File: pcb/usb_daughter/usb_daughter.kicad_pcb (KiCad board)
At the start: 2 copper layers, 26.2 x 18 mm, 6 parts, among them J1 USB-A1VSB6, J2 USB_B_Micro

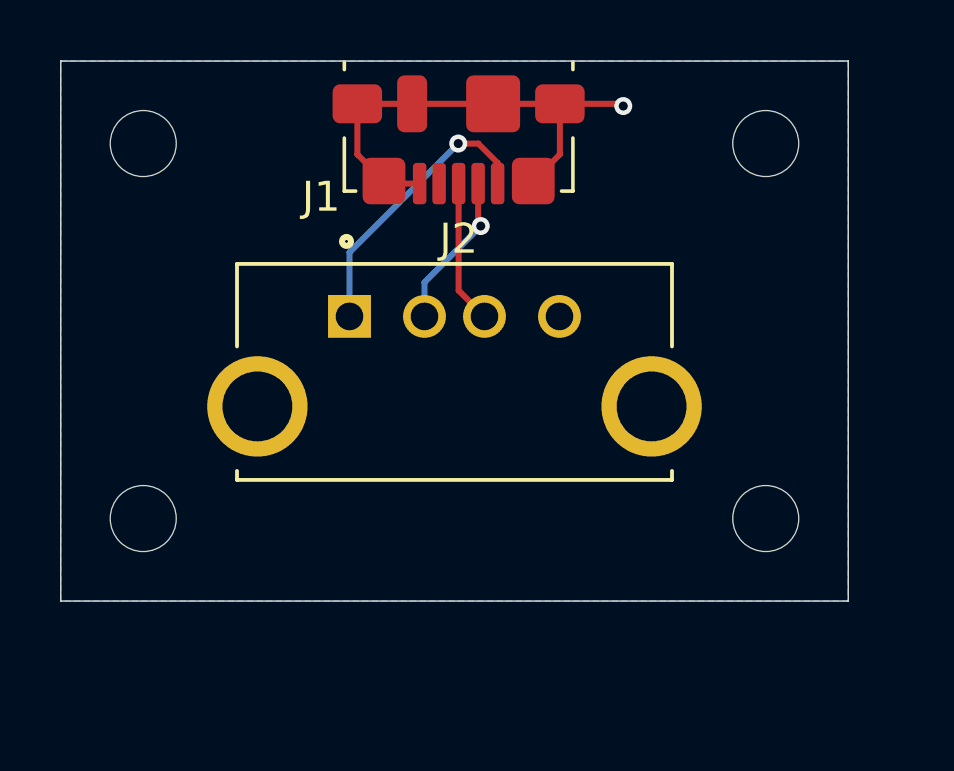
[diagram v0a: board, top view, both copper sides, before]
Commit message: Rotate footprints so that the micro usb is on the bottom realtive to how the board should be oriented
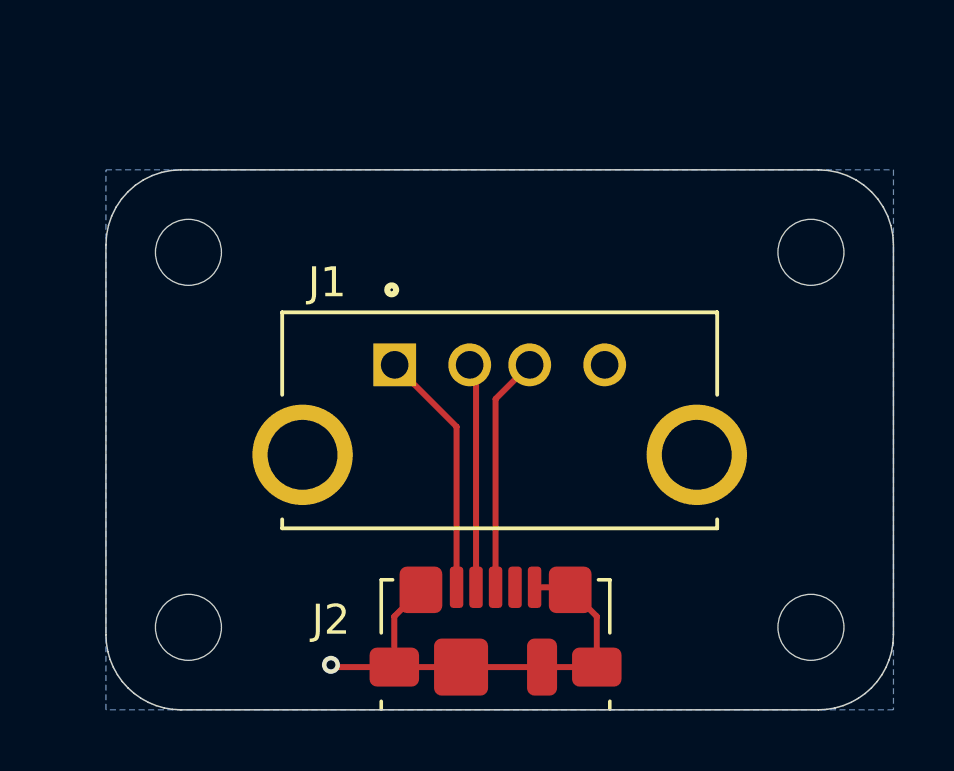
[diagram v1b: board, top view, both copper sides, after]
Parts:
- moved REF** 27.5 mm to (161.5, 102.1), turned to 180 degrees
- moved REF** 25.1 mm to (140.8, 102.1), turned to 180 degrees
- moved REF** 24.0 mm to (161.5, 89.6), turned to 180 degrees
- moved REF** 21.2 mm to (140.8, 89.6), turned to 180 degrees
- moved J2 16.4 mm to (151.0, 102.3), turned to 0 degrees
- moved J1 2.21 mm to (151.1, 96.4)
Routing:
- net Net-(J1-D+): track 4.78 -> 7.89 mm
- net Net-(J1-D-): track 5.24 -> 7.50 mm, vias 1 -> 0
- net Net-(J1-VUSB): track 9.53 -> 8.27 mm, vias 1 -> 0
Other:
- outline, holes or cut-outs redrawn
